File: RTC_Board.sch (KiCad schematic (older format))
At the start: 8 parts, among them J1 Conn_01x01, J2 Conn_01x01, J3 Conn_01x01, J4 Conn_01x01, U1 DS3231MZ

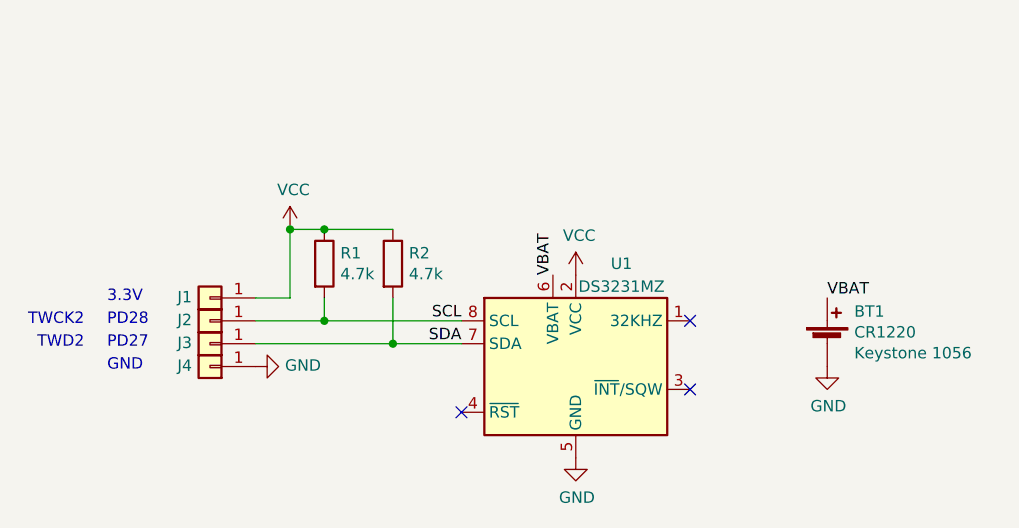
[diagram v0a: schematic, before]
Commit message: decoupling cap
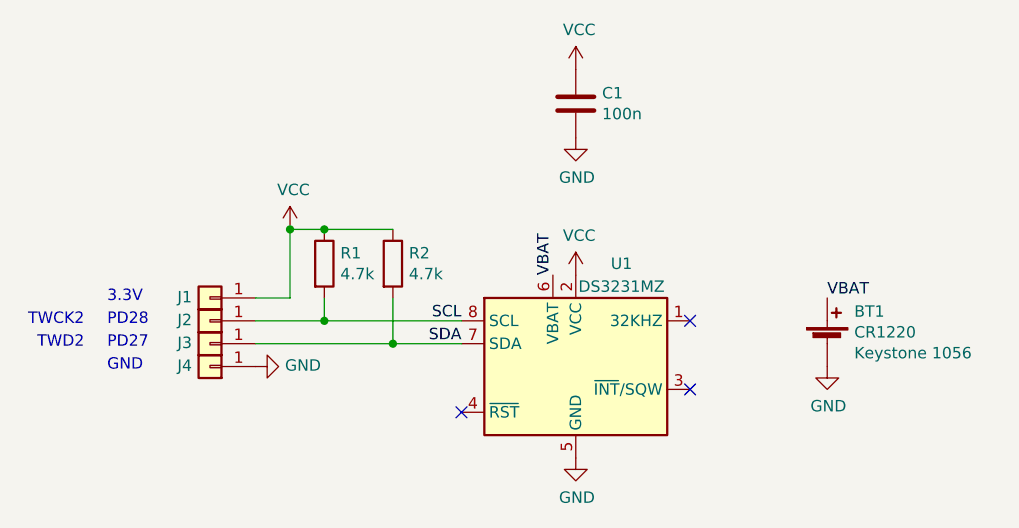
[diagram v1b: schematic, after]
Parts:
- added C1: 100n, Capacitor_SMD:C_0805_2012Metric_Pad1.15x1.40mm_HandSolder, symbol Device:C
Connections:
- net GND: now also C1.2
- net VCC: now also C1.1
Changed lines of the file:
@@
 L power:VCC #PWR0102
 U 1 1 5E4984AA
-P 5400 3400
-F 0 "#PWR0102" H 5400 3250 50  0001 C CNN
-F 1 "VCC" H 5415 3573 50  0000 C CNN
-F 2 "" H 5400 3400 50  0001 C CNN
-F 3 "" H 5400 3400 50  0001 C CNN
-	1    5400 3400
+P 5400 2500
+F 0 "#PWR0102" H 5400 2350 50  0001 C CNN
+F 1 "VCC" H 5415 2673 50  0000 C CNN
+F 2 "" H 5400 2500 50  0001 C CNN
+F 3 "" H 5400 2500 50  0001 C CNN
+	1    5400 2500
 	1    0    0    -1
 $EndComp
@@
 Text Notes 3250 3625 2    50   ~ 0
 TWCK2
+$Comp
+L power:GND #PWR0106
+U 1 1 5E4D81F6
+P 5400 2800
+F 0 "#PWR0106" H 5400 2550 50  0001 C CNN
+F 1 "GND" H 5405 2627 50  0000 C CNN
+F 2 "" H 5400 2800 50  0001 C CNN
+F 3 "" H 5400 2800 50  0001 C CNN
+	1    5400 2800
+	1    0    0    -1
+$EndComp
+$Comp
+L Device:C C1
+U 1 1 5E4D8523
+P 5400 2650
+F 0 "C1" H 5515 2696 50  0000 L CNN
+F 1 "100n" H 5515 2605 50  0000 L CNN
+F 2 "Capacitor_SMD:C_0805_2012Metric_Pad1.15x1.40mm_HandSolder" H 5438 2500 50  0001 C CNN
+F 3 "~" H 5400 2650 50  0001 C CNN
+	1    5400 2650
+	1    0    0    -1
+$EndComp
+$Comp
+L power:VCC #PWR0107
+U 1 1 5E4DAA3B
+P 5400 3400
+F 0 "#PWR0107" H 5400 3250 50  0001 C CNN
+F 1 "VCC" H 5415 3573 50  0000 C CNN
+F 2 "" H 5400 3400 50  0001 C CNN
+F 3 "" H 5400 3400 50  0001 C CNN
+	1    5400 3400
+	1    0    0    -1
+$EndComp
 $EndSCHEMATC
